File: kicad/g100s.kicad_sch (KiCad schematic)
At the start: 38 parts, among them J1 Conn_01x05_Female, J2 Conn_01x02_Female, J3 Conn_01x03_Female, SW1 SW_SPDT, SW2 SW_SPDT, SW3 SW_SPDT, SW4 SW_SPDT, SW5 SW_SPDT, SW6 SW_SPDT, SW7 SW_SPST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

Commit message: update kicad files
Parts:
- C9: value 4.7uF -> 100nF
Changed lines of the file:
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@@
     (in_bom yes) (on_board yes)
     (property "Reference" "C9" (id 0) (at 67.31 170.18 0))
-    (property "Value" "4.7uF" (id 1) (at 66.04 172.72 0))
+    (property "Value" "100nF" (id 1) (at 66.04 172.72 0))
     (property "Footprint" "Capacitor_SMD:C_0805_2012Metric_Pad1.18x1.45mm_HandSolder" (id 2) (at 70.1548 168.91 0)
       (effects (font (size 1.27 1.27)) hide)
@@
     )
     (path "/3cf9d49c-4280-4935-91dd-091ba0db3f85"
-      (reference "C9") (unit 1) (value "4.7uF") (footprint "Capacitor_SMD:C_0805_2012Metric_Pad1.18x1.45mm_HandSolder")
+      (reference "C9") (unit 1) (value "100nF") (footprint "Capacitor_SMD:C_0805_2012Metric_Pad1.18x1.45mm_HandSolder")
     )
     (path "/9ba8c4fb-6341-40cf-ac2f-0aaab8912fb1"

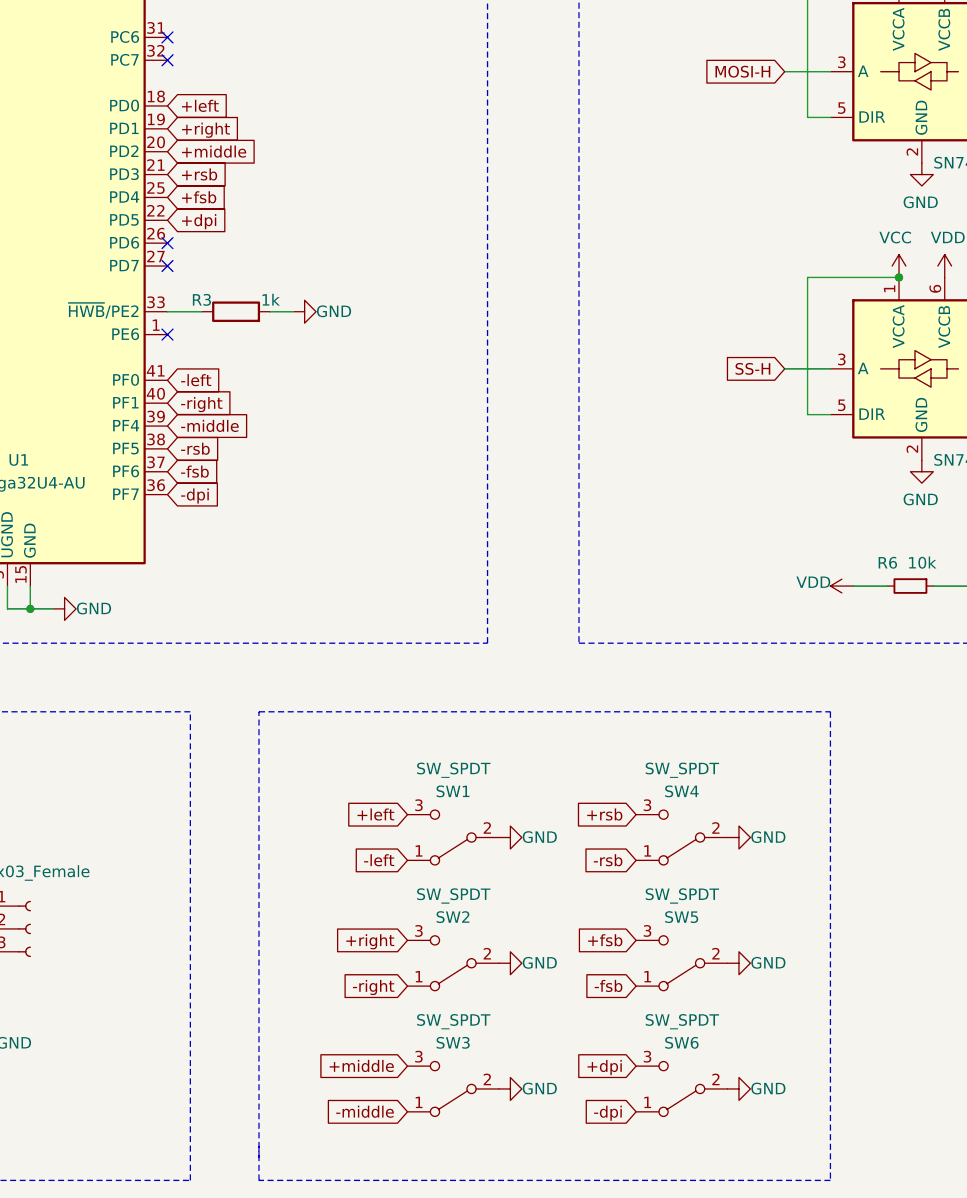
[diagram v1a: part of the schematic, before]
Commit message: remove sidebuttons
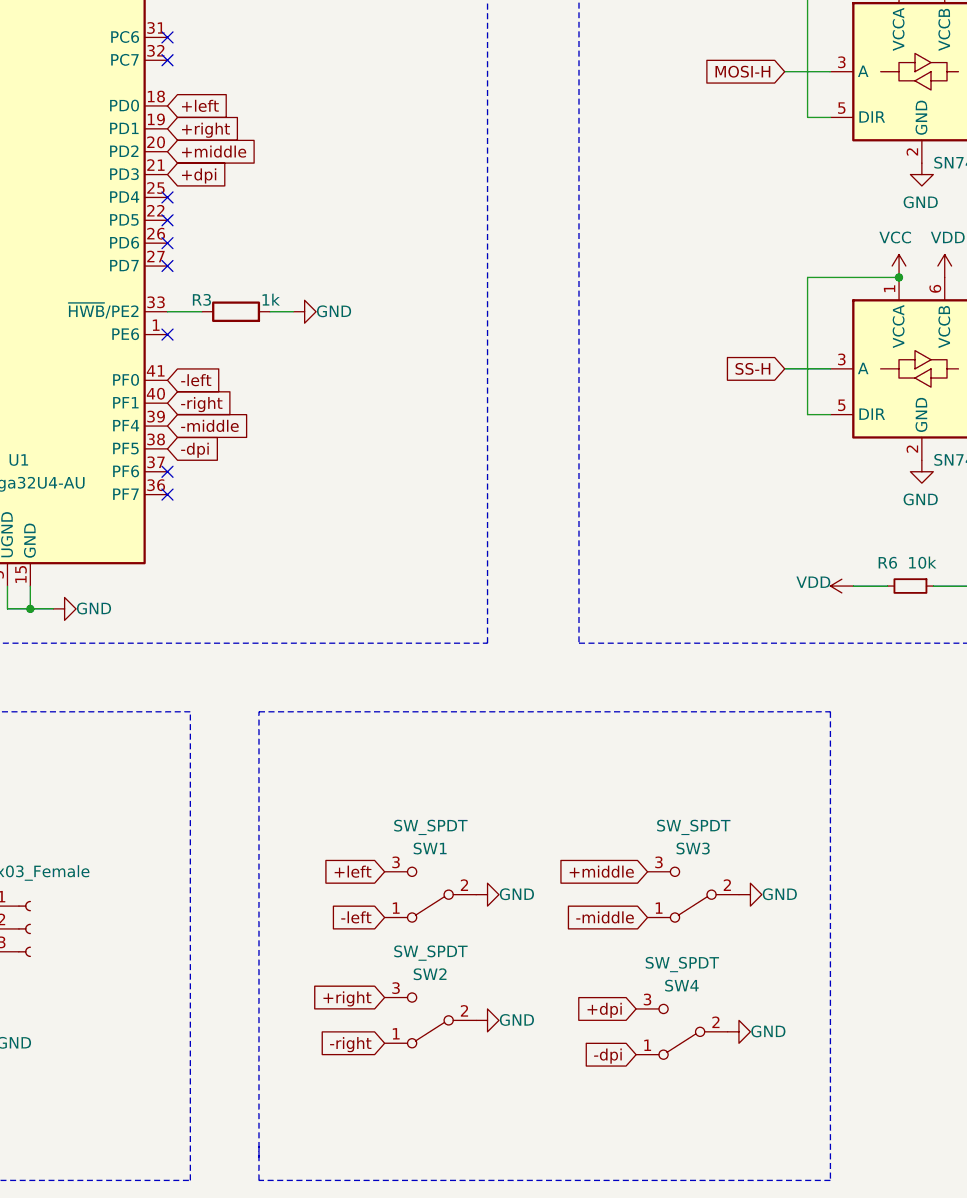
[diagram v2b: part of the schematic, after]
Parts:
- removed SW4, SW5: SW_SPDT, mouse:Microswitch_SPDT_D2F, symbol Switch:SW_SPDT
- renumbered SW6 to SW4
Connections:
- net +rsb is gone; now on net +dpi: U1.21 (PD3)
- net -rsb is gone; now on net -dpi: U1.38 (PF5)
- net +dpi: no longer U1.22 (PD5)
- net -dpi: no longer U1.36 (PF7)
- net +fsb: no longer names the net of U1.25 (PD4)
- net -fsb: no longer names the net of U1.37 (PF6)
- no-connect marks 14 -> 18
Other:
- moved on the sheet: SW1, SW2, SW3, SW4
